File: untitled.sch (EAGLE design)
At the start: 21 parts, among them IC1 ACS758LCB-050B-PFF-T

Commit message: Replace inductor with smaller one 10x10
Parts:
- removed L2: 100uH, inductors:DR125
- added L3: SRU1038, inductor-bourns:SRU1038
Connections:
- net N$9: now also L3.1; no longer L2.1
- net VCC: now also L3.2; no longer L2.2
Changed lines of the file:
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@@
 <part name="D1" library="diode" library_urn="urn:adsk.eagle:library:210" deviceset="BAT60J" device="" package3d_urn="urn:adsk.eagle:package:43461/1" value="MBRS1100T3G"/>
 <part name="GND10" library="supply1" library_urn="urn:adsk.eagle:library:371" deviceset="GND" device=""/>
-<part name="L2" library="inductors" library_urn="urn:adsk.eagle:library:243" deviceset="DR125" device="" package3d_urn="urn:adsk.eagle:package:15121/1" value="100uH "/>
 <part name="C2" library="rcl" library_urn="urn:adsk.eagle:library:334" deviceset="CPOL-EU" device="A/3216-18R" package3d_urn="urn:adsk.eagle:package:23410/2" value="2.2uF 100V"/>
 <part name="C6" library="rcl" library_urn="urn:adsk.eagle:library:334" deviceset="CPOL-EU" device="R/2012-12R" package3d_urn="urn:adsk.eagle:package:23426/2" value="22uF 25V"/>
+<part name="L3" library="inductor-bourns" deviceset="SRU1038" device=""/>
 </parts>
 <sheets>
@@
 <attribute name="VALUE" x="0" y="-45.72" size="1.778" layer="96"/>
 </instance>
-<instance part="L2" gate="G$1" x="40.64" y="-50.8" smashed="yes">
-<attribute name="NAME" x="36.83" y="-48.514" size="1.778" layer="95"/>
-<attribute name="VALUE" x="39.243" y="-56.388" size="1.778" layer="96"/>
-</instance>
 <instance part="C2" gate="G$1" x="7.62" y="35.56" smashed="yes">
 <attribute name="NAME" x="8.763" y="36.0426" size="1.778" layer="95"/>
@@
 <attribute name="NAME" x="46.863" y="36.0426" size="1.778" layer="95"/>
 <attribute name="VALUE" x="46.863" y="30.9626" size="1.778" layer="96"/>
+</instance>
+<instance part="L3" gate="G$1" x="40.64" y="-50.8" smashed="yes">
+<attribute name="NAME" x="36.83" y="-46.99" size="1.778" layer="95"/>
+<attribute name="VALUE" x="36.83" y="-53.34" size="1.778" layer="96"/>
 </instance>
 </instances>
@@
 <pinref part="P+6" gate="VCC" pin="VCC"/>
 <wire x1="53.34" y1="38.1" x2="45.72" y2="38.1" width="0.1524" layer="91"/>
-<wire x1="48.26" y1="-50.8" x2="88.9" y2="-50.8" width="0.1524" layer="91"/>
+<wire x1="45.72" y1="-50.8" x2="88.9" y2="-50.8" width="0.1524" layer="91"/>
 <wire x1="88.9" y1="-50.8" x2="88.9" y2="12.7" width="0.1524" layer="91"/>
 <pinref part="R6" gate="G$1" pin="1"/>
@@
 <wire x1="73.66" y1="38.1" x2="53.34" y2="38.1" width="0.1524" layer="91"/>
 <junction x="53.34" y="38.1"/>
-<pinref part="L2" gate="G$1" pin="2"/>
 <pinref part="C6" gate="G$1" pin="+"/>
+<pinref part="L3" gate="G$1" pin="2"/>
 </segment>
 <segment>
@@
 <wire x1="20.32" y1="-38.1" x2="20.32" y2="-50.8" width="0.1524" layer="91"/>
 <junction x="20.32" y="-38.1"/>
-<wire x1="20.32" y1="-50.8" x2="33.02" y2="-50.8" width="0.1524" layer="91"/>
+<wire x1="20.32" y1="-50.8" x2="35.56" y2="-50.8" width="0.1524" layer="91"/>
 <pinref part="D1" gate="G$1" pin="C"/>
 <wire x1="15.24" y1="-38.1" x2="20.32" y2="-38.1" width="0.1524" layer="91"/>
-<pinref part="L2" gate="G$1" pin="1"/>
-</segment>
-</net>
+<pinref part="L3" gate="G$1" pin="1"/>
+</segment>
+</net>

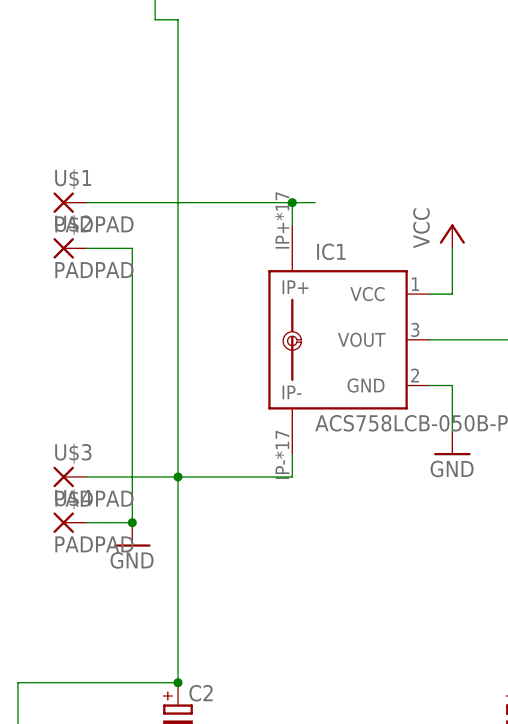
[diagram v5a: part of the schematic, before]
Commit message: Add board layout
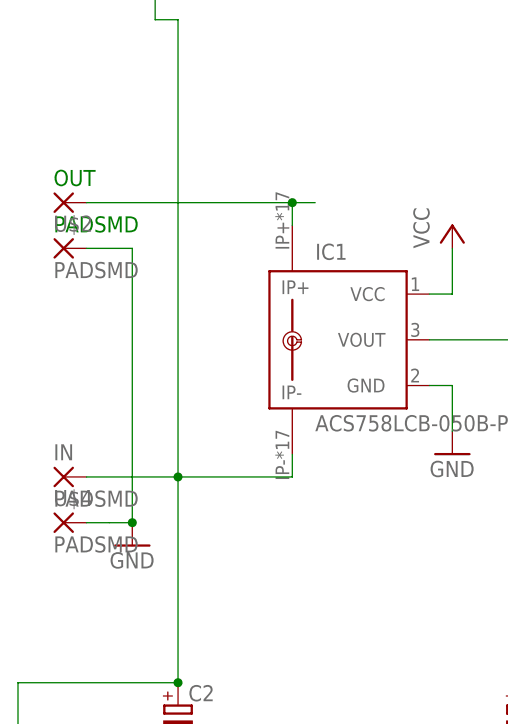
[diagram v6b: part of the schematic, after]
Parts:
- removed U$1, U$3: PADPAD, wirepad:PADPAD
- added IN, OUT: PADSMD, wirepad:PADSMD
- U$2, U$4: value PADPAD -> PADSMD; device wirepad:PADPAD -> wirepad:PADSMD
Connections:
- net N$2: now also OUT.P; no longer U$1.P
- net N$4: now also IN.P; no longer U$3.P
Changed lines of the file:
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@@
 <part name="C3" library="rcl" library_urn="urn:adsk.eagle:library:334" deviceset="C-EU" device="C0805" package3d_urn="urn:adsk.eagle:package:23617/2" value="100nF"/>
 <part name="P+7" library="supply1" library_urn="urn:adsk.eagle:library:371" deviceset="VCC" device=""/>
-<part name="U$1" library="wirepad" deviceset="PAD" device="PAD" value="PADPAD"/>
-<part name="U$2" library="wirepad" deviceset="PAD" device="PAD" value="PADPAD"/>
-<part name="U$3" library="wirepad" deviceset="PAD" device="PAD" value="PADPAD"/>
-<part name="U$4" library="wirepad" deviceset="PAD" device="PAD" value="PADPAD"/>
+<part name="OUT" library="wirepad" deviceset="PAD" device="SMD" value="PADSMD"/>
+<part name="U$2" library="wirepad" deviceset="PAD" device="SMD" value="PADSMD"/>
+<part name="IN" library="wirepad" deviceset="PAD" device="SMD" value="PADSMD"/>
+<part name="U$4" library="wirepad" deviceset="PAD" device="SMD" value="PADSMD"/>
 <part name="GND7" library="supply1" library_urn="urn:adsk.eagle:library:371" deviceset="GND" device=""/>
 <part name="GND8" library="supply1" library_urn="urn:adsk.eagle:library:371" deviceset="GND" device=""/>
@@
 <attribute name="VALUE" x="134.62" y="86.36" size="1.778" layer="96" rot="R90"/>
 </instance>
-<instance part="U$1" gate="G$1" x="-5.08" y="91.44" smashed="yes">
-<attribute name="NAME" x="-6.223" y="93.2942" size="1.778" layer="95"/>
-<attribute name="VALUE" x="-6.223" y="88.138" size="1.778" layer="96"/>
+<instance part="OUT" gate="G$1" x="-5.08" y="91.44" smashed="yes">
+<attribute name="NAME" x="-6.223" y="93.2942" size="1.778" layer="91"/>
+<attribute name="VALUE" x="-6.223" y="88.138" size="1.778" layer="91"/>
 </instance>
 <instance part="U$2" gate="G$1" x="-5.08" y="86.36" smashed="yes">
@@
 <attribute name="VALUE" x="-6.223" y="83.058" size="1.778" layer="96"/>
 </instance>
-<instance part="U$3" gate="G$1" x="-5.08" y="60.96" smashed="yes">
+<instance part="IN" gate="G$1" x="-5.08" y="60.96" smashed="yes">
 <attribute name="NAME" x="-6.223" y="62.8142" size="1.778" layer="95"/>
 <attribute name="VALUE" x="-6.223" y="57.658" size="1.778" layer="96"/>
@@
 <wire x1="5.08" y1="111.76" x2="5.08" y2="116.84" width="0.1524" layer="91"/>
 <wire x1="7.62" y1="60.96" x2="7.62" y2="38.1" width="0.1524" layer="91"/>
-<pinref part="U$3" gate="G$1" pin="P"/>
+<pinref part="IN" gate="G$1" pin="P"/>
 <wire x1="7.62" y1="38.1" x2="-10.16" y2="38.1" width="0.1524" layer="91"/>
 <wire x1="-10.16" y1="38.1" x2="-10.16" y2="-10.16" width="0.1524" layer="91"/>
@@
 <junction x="20.32" y="91.44"/>
 <wire x1="-2.54" y1="91.44" x2="20.32" y2="91.44" width="0.1524" layer="91"/>
-<pinref part="U$1" gate="G$1" pin="P"/>
-</segment>
-</net>
+<pinref part="OUT" gate="G$1" pin="P"/>
+</segment>
+</net>

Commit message: Update board layout based on bought components
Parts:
- C2: device rcl:CPOL-EUA/3216-18R -> rcl:CPOL-EUB/3528-21R
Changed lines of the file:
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@@
 <part name="D1" library="diode" library_urn="urn:adsk.eagle:library:210" deviceset="BAT60J" device="" package3d_urn="urn:adsk.eagle:package:43461/1" value="MBRS1100T3G"/>
 <part name="GND10" library="supply1" library_urn="urn:adsk.eagle:library:371" deviceset="GND" device=""/>
-<part name="C2" library="rcl" library_urn="urn:adsk.eagle:library:334" deviceset="CPOL-EU" device="A/3216-18R" package3d_urn="urn:adsk.eagle:package:23410/2" value="2.2uF 100V"/>
+<part name="C2" library="rcl" library_urn="urn:adsk.eagle:library:334" deviceset="CPOL-EU" device="B/3528-21R" package3d_urn="urn:adsk.eagle:package:23409/2" value="2.2uF 100V"/>
 <part name="C6" library="rcl" library_urn="urn:adsk.eagle:library:334" deviceset="CPOL-EU" device="R/2012-12R" package3d_urn="urn:adsk.eagle:package:23426/2" value="22uF 25V"/>
 <part name="L3" library="inductor-bourns" deviceset="SRU1038" device=""/>
